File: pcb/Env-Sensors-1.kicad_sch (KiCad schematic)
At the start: 17 parts, among them J1 SEN66, U10 SCD41, U14 SHT45, U9 SGP41

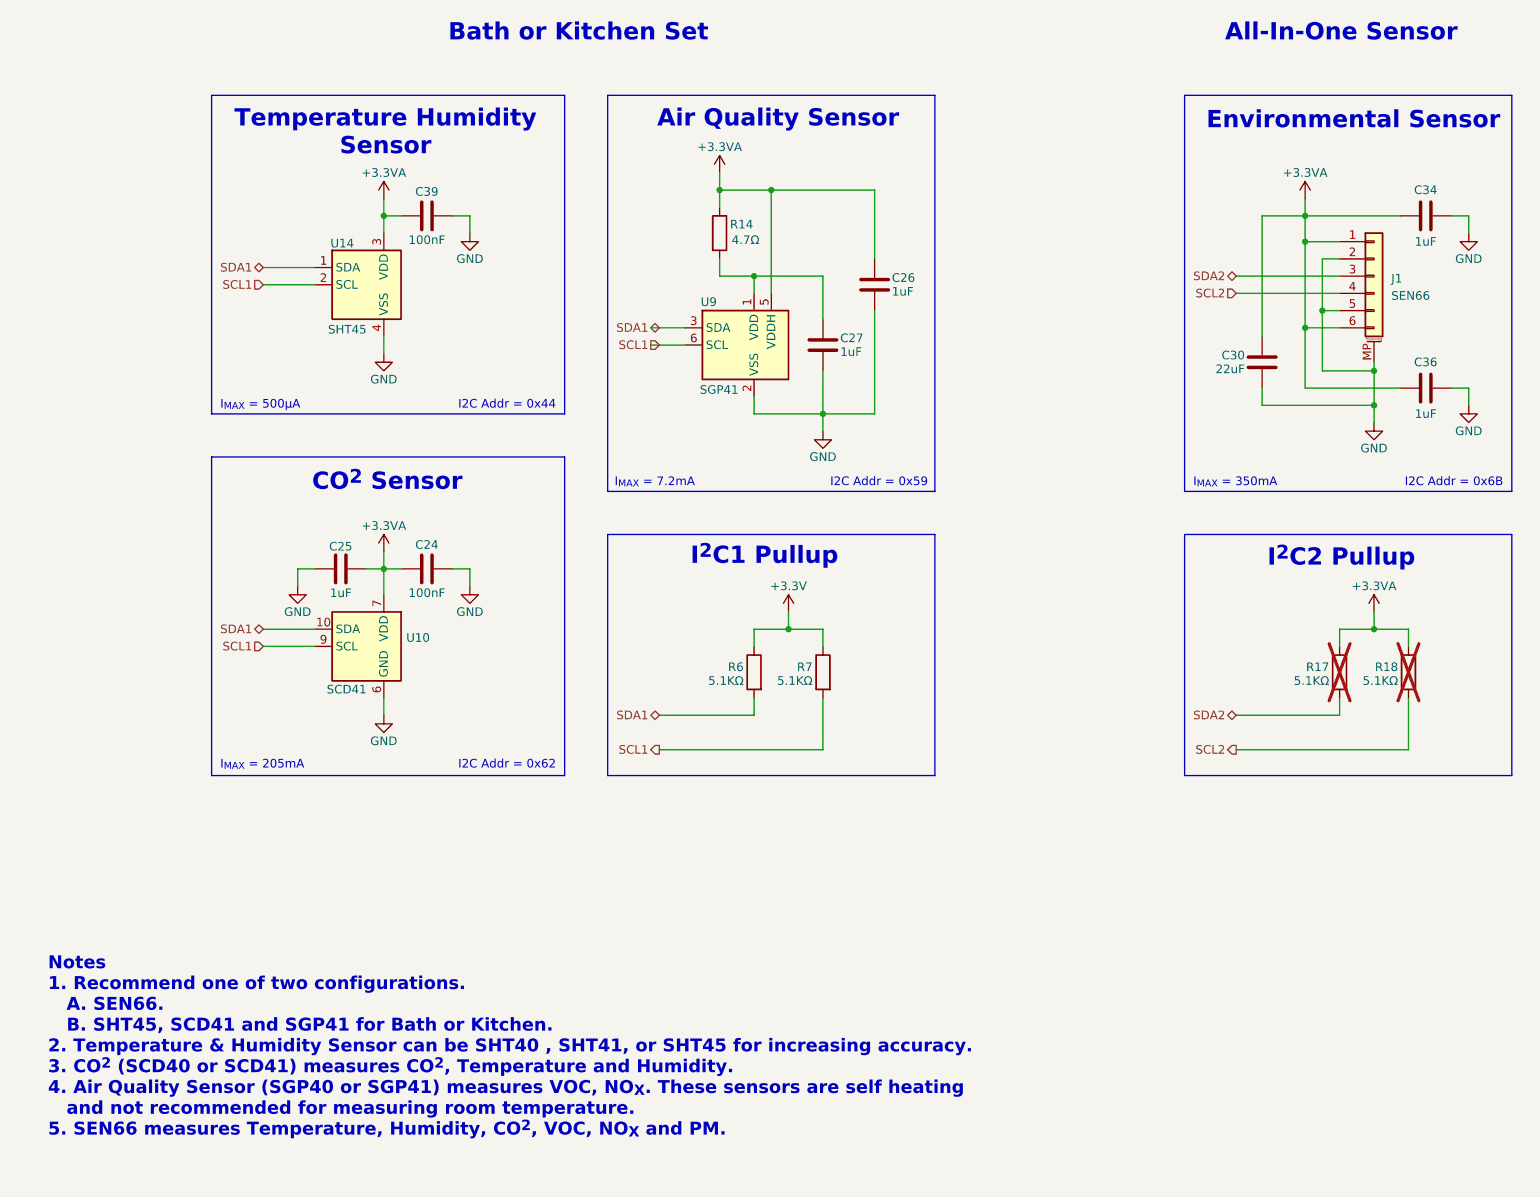
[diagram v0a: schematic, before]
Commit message: Rev B Updates finish adding power monitors for 3.3V and 3.3VA
Removed speaker gain jumper
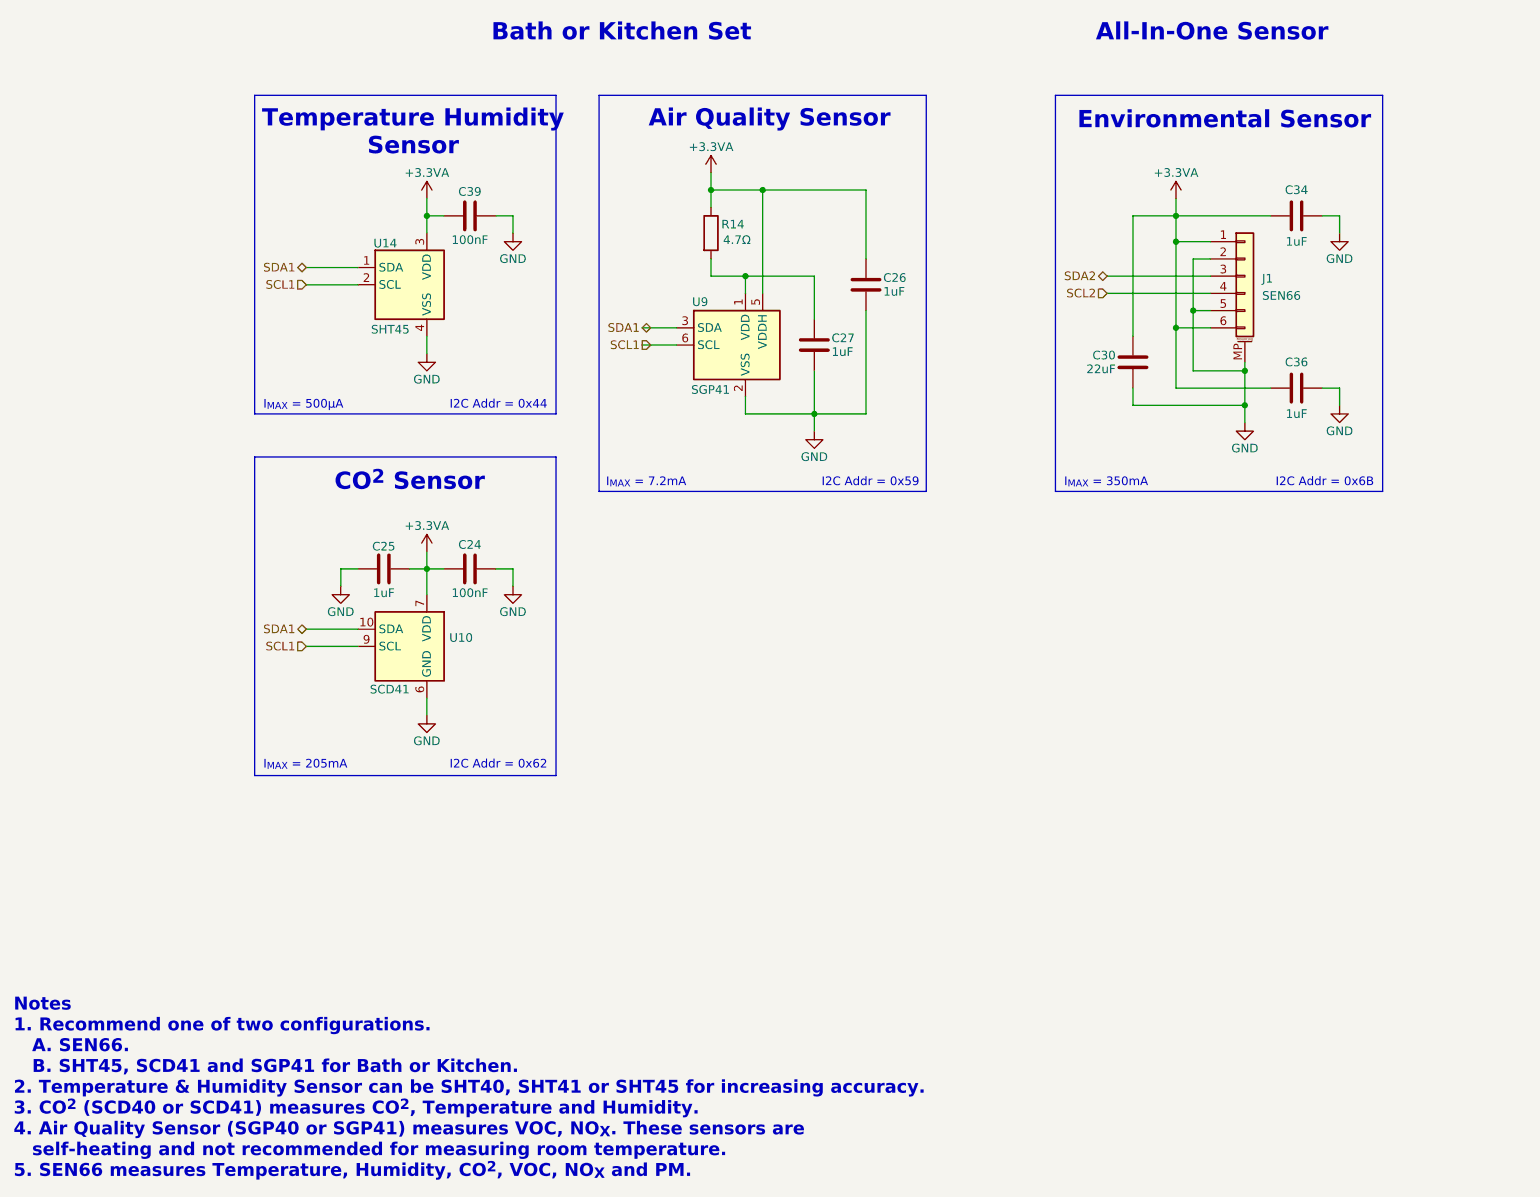
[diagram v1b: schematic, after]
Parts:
- removed R17, R18, R6, R7: 5.1KΩ, Resistor_SMD:R_0402_1005Metric, symbol Device:R
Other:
- note added: "Notes 1. Recommend one of two configurations. A. SEN66. B. SHT45, SCD41 and SGP41 for Bath or Kitchen. 2. Temperature & Humidity Sensor can be SHT40, SHT41 or SHT45 for increasing accuracy. 3. CO^{2} (SCD40 or SCD41) measures CO^{2}, Temperature and Humidity. 4. Air Quality Sensor (SGP40 or SGP41) measures VOC, NO_{X}. These sensors are self-heating and not recommended for measuring room temperat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"
- note removed: "I^{2}C1 Pullup"
- note removed: "I^{2}C2 Pullup"
- note removed: "Notes 1. Recommend one of two configurations. A. SEN66. B. SHT45, SCD41 and SGP41 for Bath or Kitchen. 2. Temperature & Humidity Sensor can be SHT40 , SHT41, or SHT45 for increasing accuracy. 3. CO^{2} (SCD40 or SCD41) measures CO^{2}, Temperature and Humidity. 4. Air Quality Sensor (SGP40 or SGP41) measures VOC, NO_{X}. These sensors are self heating and not recommended for measuring room temper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"
- title: ESPHome Parking Assistant -> ESPHome Indoor Multi-Sensor
- moved on the sheet: C24, C25, C26, C27, C30, C34, C36, C39, J1, R14, U10, U14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
